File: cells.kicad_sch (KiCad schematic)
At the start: 2 parts, among them J7 Conn_01x10_Pin, J8 Conn_01x02_Pin

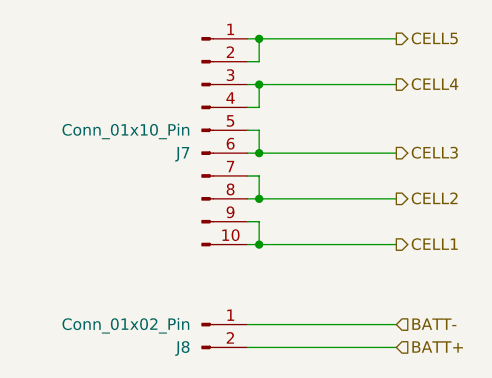
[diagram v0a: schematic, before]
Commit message: Adding in JST XH
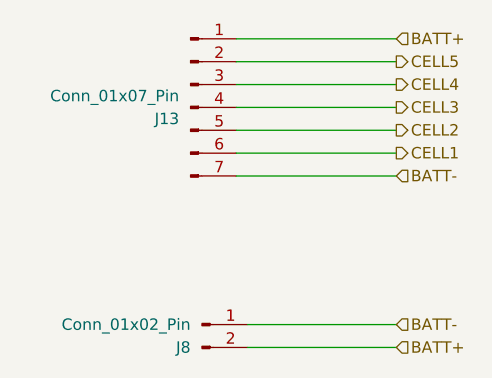
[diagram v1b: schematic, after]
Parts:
- removed J7: Conn_01x10_Pin, _BMS:TB4-Hirose, symbol Connector:Conn_01x10_Pin
- added J13: Conn_01x07_Pin, Connector_JST:JST_XH_S7B-XH-A-1_1x07_P2.50mm_Horizontal, symbol Connector:Conn_01x07_Pin
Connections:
- net BATT+: now also J13.1 (Pin_1)
- net BATT-: now also J13.7 (Pin_7)
- net CELL1: now also J13.6 (Pin_6)
- net CELL2: now also J13.5 (Pin_5)
- net CELL3: now also J13.4 (Pin_4)
- net CELL4: now also J13.3 (Pin_3)
- net CELL5: now also J13.2 (Pin_2)
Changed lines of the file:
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@@
 		(comment 3 "Reviewer 2:")
 	)
-	(junction
-		(at 125.73 97.79)
-		(diameter 0)
-		(color 0 0 0 0)
-	)
-	(junction
-		(at 125.73 87.63)
-		(diameter 0)
-		(color 0 0 0 0)
-	)
-	(junction
-		(at 125.73 80.01)
-		(diameter 0)
-		(color 0 0 0 0)
-	)
-	(junction
-		(at 125.73 74.93)
-		(diameter 0)
-		(color 0 0 0 0)
-	)
-	(junction
-		(at 125.73 92.71)
-		(diameter 0)
-		(color 0 0 0 0)
-	)
-	(wire
-		(pts
-			(xy 125.73 95.25) (xy 125.73 97.79)
-		)
-		(stroke
-			(width 0)
-			(type default)
-		)
-	)
-	(wire
-		(pts
-			(xy 124.46 80.01) (xy 125.73 80.01)
-		)
-		(stroke
-			(width 0)
-			(type default)
-		)
-	)
-	(wire
-		(pts
-			(xy 125.73 90.17) (xy 125.73 92.71)
-		)
-		(stroke
-			(width 0)
-			(type default)
-		)
-	)
-	(wire
-		(pts
-			(xy 124.46 82.55) (xy 125.73 82.55)
-		)
-		(stroke
-			(width 0)
-			(type default)
-		)
-	)
-	(wire
-		(pts
-			(xy 124.46 95.25) (xy 125.73 95.25)
+	(wire
+		(pts
+			(xy 123.19 80.01) (xy 140.97 80.01)
+		)
+		(stroke
+			(width 0)
+			(type default)
+		)
+	)
+	(wire
+		(pts
+			(xy 123.19 77.47) (xy 140.97 77.47)
+		)
+		(stroke
+			(width 0)
+			(type default)
+		)
+	)
+	(wire
+		(pts
+			(xy 123.19 90.17) (xy 140.97 90.17)
 		)
 		(stroke
@@
 	(wire
 		(pts
-			(xy 125.73 97.79) (xy 140.97 97.79)
-		)
-		(stroke
-			(width 0)
-			(type default)
-		)
-	)
-	(wire
-		(pts
-			(xy 125.73 74.93) (xy 125.73 77.47)
-		)
-		(stroke
-			(width 0)
-			(type default)
-		)
-	)
-	(wire
-		(pts
-			(xy 124.46 97.79) (xy 125.73 97.79)
-		)
-		(stroke
-			(width 0)
-			(type default)
-		)
-	)
-	(wire
-		(pts
-			(xy 124.46 74.93) (xy 125.73 74.93)
-		)
-		(stroke
-			(width 0)
-			(type default)
-		)
-	)
-	(wire
-		(pts
-			(xy 125.73 87.63) (xy 140.97 87.63)
-		)
-		(stroke
-			(width 0)
-			(type default)
-		)
-	)
-	(wire
-		(pts
-			(xy 125.73 74.93) (xy 140.97 74.93)
-		)
-		(stroke
-			(width 0)
-			(type default)
-		)
-	)
-	(wire
-		(pts
-			(xy 124.46 85.09) (xy 125.73 85.09)
-		)
-		(stroke
-			(width 0)
-			(type default)
-		)
-	)
-	(wire
-		(pts
-			(xy 124.46 87.63) (xy 125.73 87.63)
-		)
-		(stroke
-			(width 0)
-			(type default)
-		)
-	)
-	(wire
-		(pts
-			(xy 125.73 92.71) (xy 140.97 92.71)
-		)
-		(stroke
-			(width 0)
-			(type default)
-		)
-	)
-	(wire
-		(pts
-			(xy 124.46 77.47) (xy 125.73 77.47)
-		)
-		(stroke
-			(width 0)
-			(type default)
-		)
-	)
-	(wire
-		(pts
-			(xy 124.46 90.17) (xy 125.73 90.17)
-		)
-		(stroke
-			(width 0)
-			(type default)
-		)
-	)
-	(wire
-		(pts
-			(xy 125.73 80.01) (xy 125.73 82.55)
+			(xy 123.19 87.63) (xy 140.97 87.63)
+		)
+		(stroke
+			(width 0)
+			(type default)
+		)
+	)
+	(wire
+		(pts
+			(xy 123.19 85.09) (xy 140.97 85.09)
+		)
+		(stroke
+			(width 0)
+			(type default)
+		)
+	)
+	(wire
+		(pts
+			(xy 123.19 82.55) (xy 140.97 82.55)
 		)
 		(stroke
@@
 	(wire
 		(pts
-			(xy 125.73 85.09) (xy 125.73 87.63)
-		)
-		(stroke
-			(width 0)
-			(type default)
-		)
-	)
-	(wire
-		(pts
-			(xy 124.46 92.71) (xy 125.73 92.71)
-		)
-		(stroke
-			(width 0)
-			(type default)
-		)
-	)
-	(wire
-		(pts
-			(xy 125.73 80.01) (xy 140.97 80.01)
+			(xy 123.19 74.93) (xy 140.97 74.93)
 		)
 		(stroke
@@
 		)
 	)
+	(hierarchical_label "BATT-"
+		(shape input)
+		(at 140.97 90.17 0)
+		(effects
+			(font
+				(size 1.27 1.27)
+			)
+			(justify left)
+		)
+	)
 	(hierarchical_label "CELL1"
 		(shape output)
-		(at 140.97 97.79 0)
+		(at 140.97 87.63 0)
 		(effects
 			(font
@@
 	(hierarchical_label "CELL3"
 		(shape output)
-		(at 140.97 87.63 0)
+		(at 140.97 82.55 0)
+		(effects
+			(font
+				(size 1.27 1.27)
+			)
+			(justify left)
+		)
+	)
+	(hierarchical_label "BATT+"
+		(shape input)
+		(at 140.97 74.93 0)
 		(effects
 			(font
@@
 	(hierarchical_label "CELL5"
 		(shape output)
-		(at 140.97 74.93 0)
+		(at 140.97 77.47 0)
 		(effects
 			(font
@@
 	(hierarchical_label "CELL2"
 		(shape output)
-		(at 140.97 92.71 0)
+		(at 140.97 85.09 0)
 		(effects
 			(font
@@
 	)
 	(symbol
-		(lib_id "Connector:Conn_01x10_Pin")
-		(at 119.38 85.09 0)
+		(lib_id "Connector:Conn_01x07_Pin")
+		(at 118.11 82.55 0)
 		(unit 1)
 		(exclude_from_sim no)
-		(in_bom no)
+		(in_bom yes)
 		(on_board yes)
 		(dnp no)
-		(property "Reference" "J7"
-			(at 118.11 87.6301 0)
+		(property "Reference" "J13"
+			(at 116.84 83.8201 0)
 			(effects
 				(font
@@
 			)
 		)
-		(property "Value" "Conn_01x10_Pin"
-			(at 118.11 85.0901 0)
+		(property "Value" "Conn_01x07_Pin"
+			(at 116.84 81.2801 0)
 			(effects
 				(font
@@
 			)
 		)
-		(property "Footprint" "_BMS:TB4-Hirose"
-			(at 119.38 85.09 0)
+		(property "Footprint" "Connector_JST:JST_XH_S7B-XH-A-1_1x07_P2.50mm_Horizontal"
+			(at 118.11 82.55 0)
 			(effects
 				(font
@@
 		)
 		(property "Datasheet" "~"
-			(at 119.38 85.09 0)
-			(effects
-				(font
-					(size 1.27 1.27)
-				)
-				(hide yes)
-			)
-		)
-		(property "Description" "Generic connector, single row, 01x10, script generated"
-			(at 119.38 85.09 0)
+			(at 118.11 82.55 0)
+			(effects
+				(font
+					(size 1.27 1.27)
+				)
+				(hide yes)
+			)
+		)
+		(property "Description" "Generic connector, single row, 01x07, script generated"
+			(at 118.11 82.55 0)
 			(effects
 				(font
@@
 		)
 		(property "Mfr" ""
-			(at 119.38 85.09 0)
+			(at 118.11 82.55 0)
 			(effects
 				(font
@@
 		)
 		(property "Mfr P/N" ""
-			(at 119.38 85.09 0)
+			(at 118.11 82.55 0)
 			(effects
 				(font
@@
 		)
 		(property "Supplier_1" ""
-			(at 119.38 85.09 0)
+			(at 118.11 82.55 0)
 			(effects
 				(font
@@
 		)
 		(property "Supplier_1 P/N" ""
-			(at 119.38 85.09 0)
+			(at 118.11 82.55 0)
 			(effects
 				(font
@@
 		)
 		(property "Supplier_1 Unit Price" ""
-			(at 119.38 85.09 0)
+			(at 118.11 82.55 0)
 			(effects
 				(font
@@
 		)
 		(property "Supplier_1 Price @ Qty" ""
-			(at 119.38 85.09 0)
+			(at 118.11 82.55 0)
 			(effects
 				(font
@@
 		)
 		(property "Supplier_2" ""
-			(at 119.38 85.09 0)
+			(at 118.11 82.55 0)
 			(effects
 				(font
@@
 		)
 		(property "Supplier_2 P/N" ""
-			(at 119.38 85.09 0)
+			(at 118.11 82.55 0)
 			(effects
 				(font
@@
 		)
 		(property "Supplier_2 Unit Price" ""
-			(at 119.38 85.09 0)
+			(at 118.11 82.55 0)
 			(effects
 				(font
@@
 		)
 		(property "Supplier_2 Price @ Qty" ""
-			(at 119.38 85.09 0)
-			(effects
-				(font
-					(size 1.27 1.27)
-				)
-				(hide yes)
-			)
-		)
-		(property "DigiKey_Part_Number" ""
-			(at 119.38 85.09 0)
-			(effects
-				(font
-					(size 1.27 1.27)
-				)
-				(hide yes)
-			)
+			(at 118.11 82.55 0)
+			(effects
+				(font
+					(size 1.27 1.27)
+				)
+				(hide yes)
+			)
+		)
+		(pin "6"
+		)
+		(pin "7"
+		)
+		(pin "2"
+		)
+		(pin "3"
 		)
 		(pin "5"
 		)
-		(pin "8"
-		)
-		(pin "9"
-		)
-		(pin "7"
-		)
-		(pin "6"
+		(pin "1"
 		)
 		(pin "4"
-		)
-		(pin "1"
-		)
-		(pin "3"
-		)
-		(pin "2"
-		)
-		(pin "10"
 		)
 		(instances
 			(project ""
 				(path "/124184ba-5d68-4d9f-8da6-acc6720ab30b/93f9b420-7cce-46a9-9201-666f07a18f85/72bfe5e0-3464-488b-90f8-8143600a08cb"
-					(reference "J7")
+					(reference "J13")
 					(unit 1)
 				)

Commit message: Adding JST XH and moving test points
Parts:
- J13: Mfr (none) -> JST; Mfr P/N (none) -> S7B-XH-A(LF)(SN); Supplier_2 (none) -> JLCPCB; Supplier_2 P/N (none) -> C157916
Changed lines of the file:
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@@
 			)
 		)
-		(property "Mfr" ""
+		(property "Mfr" "JST"
 			(at 118.11 82.55 0)
 			(effects
@@
 			)
 		)
-		(property "Mfr P/N" ""
+		(property "Mfr P/N" "S7B-XH-A(LF)(SN)"
 			(at 118.11 82.55 0)
 			(effects
@@
 			)
 		)
-		(property "Supplier_2" ""
+		(property "Supplier_2" "JLCPCB"
 			(at 118.11 82.55 0)
 			(effects
@@
 			)
 		)
-		(property "Supplier_2 P/N" ""
+		(property "Supplier_2 P/N" "C157916"
 			(at 118.11 82.55 0)
 			(effects
